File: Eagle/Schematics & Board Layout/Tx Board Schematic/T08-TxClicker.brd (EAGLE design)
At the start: 88.9 x 44.5 mm, 86 parts, among them U1 CC430F513X---RGZ48, Y1 26MHz

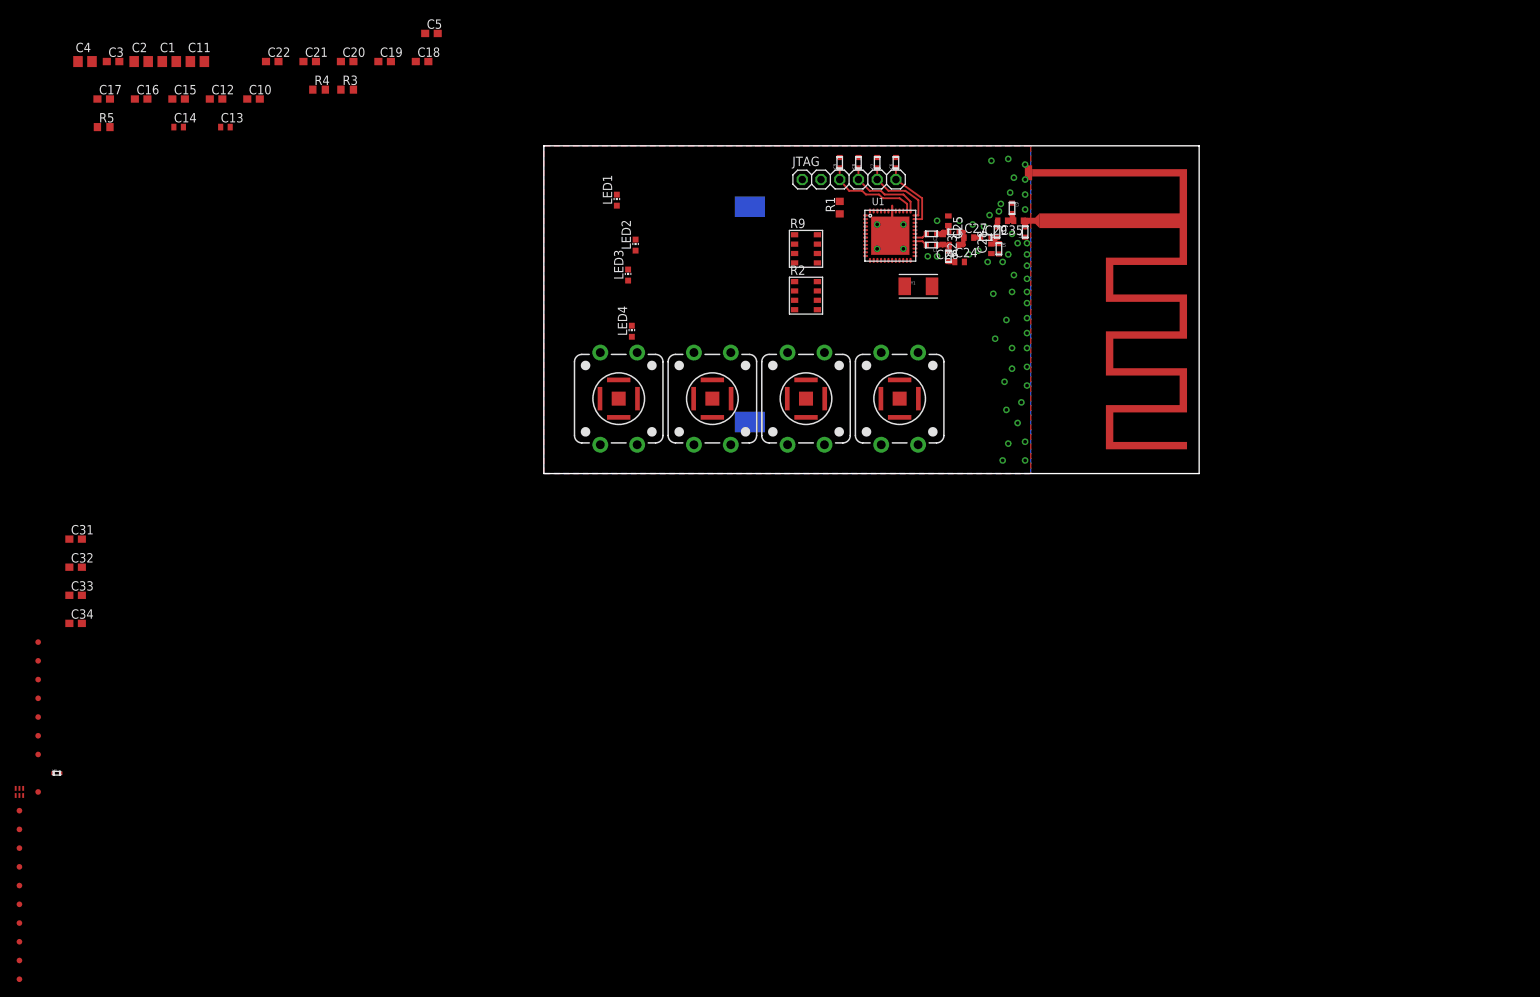
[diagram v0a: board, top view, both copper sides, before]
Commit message: Eagle BRD Layout
Incomplete, first pass layout
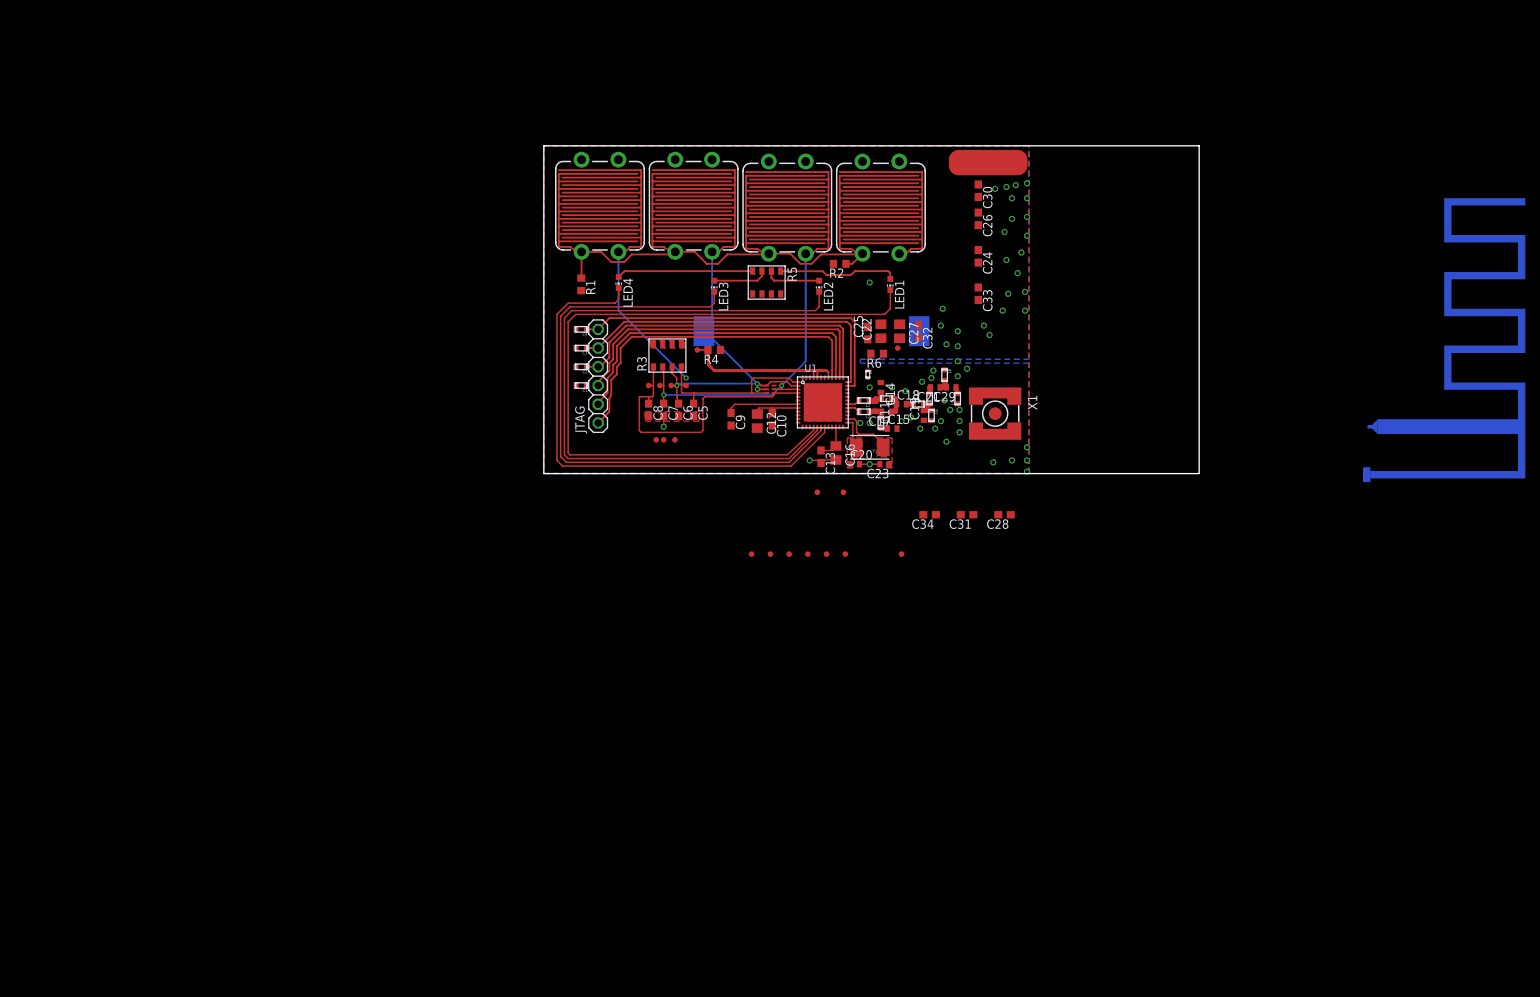
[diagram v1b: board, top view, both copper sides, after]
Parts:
- removed C35: 16pF, rcl:C0402
- removed R9: 10MEG, QuadResistor:2012(4_RES)
- removed U$1, U$3, U$4: TOUCH-PAD, TouchPad:TOUCH-PAD
- removed U$2: CR2032-SNAPDRAGONCR2032, CR2032-SnapDragon:CR2032-SNAPDRAGON
- removed U$7: PCB_ANTENNA_915MHZOSHP, PCB_Antenna_915MHz-halseth:PCB_ANTENNA_915MHZ
- added C30: 2pF, rcl:C0603
- added GND: (no value), SparkFun-Connectors:STARBOARD_GROUND_SMALL2
- added R6: 56k, rcl:R0603
- added U$6: PCB_ANTENNA_915MHZOSHP, PCB_Antenna_915MHz-halseth:PCB_ANTENNA_915MHZ
- added X1: SMA-SMD, con-coax:SMA-SMD
- C1: value 10uF -> 2nF; device rcl:C0805 -> rcl-amber:C0603
- C11: value 10uF -> 1pF; device rcl:C0805 -> rcl:C0402
- C12, C16: value 100nF -> 10uF; device rcl:C0603 -> rcl:C0805
- C13: value 18pF -> 100nF; device rcl:C0402 -> rcl:C0603
- C14: value 18pF -> 1.5pF
- C15: value 100nF -> 100pF; device rcl:C0603 -> rcl:C0402
- C17: value 2pF -> 1.5pF; device rcl:C0603 -> rcl:C0402
- C18, C21: value 100nF -> 1.5pF; device rcl:C0603 -> rcl:C0402
- C19: value 2pF -> 8.2pF; device rcl:C0603 -> rcl:C0402
- C2, C4: value 10uF -> 2pF; device rcl:C0805 -> rcl-amber:C0603
- C20: value 100nF -> 18pF; device rcl:C0603 -> rcl:C0402
- C22: value 470nF -> 10uF; device rcl:C0603 -> rcl:C0805
- C23: value 1pF -> 18pF
- C24: value 100pF -> 100nF; device rcl:C0402 -> rcl:C0603
- C25, C26: value 1.5pF -> 100nF; device rcl:C0402 -> rcl:C0603
- C27: value 1.5pF -> 10uF; device rcl:C0402 -> rcl:C0805
- C28: value 8.2pF -> 100nF; device rcl:C0402 -> rcl:C0603
- C29: value 1.5pF -> 16pF
- C3: value 100nF -> 2pF; device rcl:C0603 -> rcl-amber:C0603
- C31, C32, C33: value DNI -> 100nF
- C34: value DNI -> 2pF
- C5: value 100nF -> DNI
- C6, C7, C8: value 2pF -> DNI; device rcl-amber:C0603 -> rcl:C0603
- C9: value 2nF -> 470nF; device rcl-amber:C0603 -> rcl:C0603
- L8: value 5.6nH -> DNP
- L9: value DNP -> 5.6nH
- R1: value 47k -> 10k
- R2: value 3.3k -> DNI; device QuadResistor:2012(4_RES) -> rcl:R0603
- R3: value 56k -> 10MEG; device rcl:R0603 -> QuadResistor:2012(4_RES)
- R4: value 10k -> 47k
- R5: value DNI -> 3.3k; device rcl:R0603 -> QuadResistor:2012(4_RES)
- S1, S2, S3, S4: value SWITCH-MOMENTARY-212MM -> TOUCHPAD_SWITCH_COMBOSWITC_TOUCHPAD; device SparkFun-Electromechanical:TACTILE-PTH-12MM -> SparkFun-Electromechanical--edited:TACTILE-PTH-12MM
- U$5: value TOUCH-PAD -> CR2032-SNAPDRAGONCR2032; device TouchPad:TOUCH-PAD -> CR2032-SnapDragon:CR2032-SNAPDRAGON
- moved TP18 146.7 mm to (48.0, 17.0), turned to 90 degrees
- moved C33 129.1 mm to (58.9, 24.4), turned to 270 degrees
- moved TP9 124.6 mm to (48.5, -10.9), turned to 270 degrees
- moved L10 122.6 mm to (43.9, 13.5), turned to 270 degrees
- moved C31 120.9 mm to (57.4, -5.59), turned to 180 degrees
- moved TP10 120.8 mm to (40.6, -2.54), turned to 270 degrees
- moved TP12 119.8 mm to (40.9, -10.9), turned to 270 degrees
- moved C32 118.7 mm to (50.8, 19.3), turned to 270 degrees
- moved TP11 118.5 mm to (37.1, -2.54), turned to 270 degrees
- moved TP13 118.3 mm to (38.4, -10.9), turned to 270 degrees
- moved TP14 117.0 mm to (35.8, -10.9), turned to 270 degrees
- moved C34 116.8 mm to (52.3, -5.59), turned to 180 degrees
- moved TP15 115.8 mm to (33.3, -10.9), turned to 270 degrees
- moved D1 115.6 mm to (30.7, 11.4), turned to 270 degrees
- moved TP16 114.6 mm to (30.7, -10.9), turned to 270 degrees
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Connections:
- removed net N$10: C35.1, L8.2, U$7.ANT
- removed net N$12: TP9.P$1
- removed net N$18: LED1.A, R2.1
- removed net N$21: LED3.A, R2.7
- removed net N$23: LED4.A, R2.5
- removed net N$24: LED2.A, R2.3
- new net ANTENNA: C29.1, L9.2, U$6.ANT, X1.1
- new net N$13: LED1.A, R5.7
- new net N$14: LED2.A, R5.5
- new net N$16: LED3.A, R5.3
- new net N$17: LED4.A, R5.1
- net GND: now also C14.1, C19.1, C23.2, C25.2, C26.2, C27.2, C28.2, C30.2, R2.2, R3.2, R3.4, R3.6, R3.8, R6.1, U$5.V-, U$6.GPLANE, X1.2@1, X1.2@2, X1.2@3, X1.2@4, X1.2@5, X1.2@6; no longer C11.2, C14.2, C17.2, C18.2, C19.2, C21.2, C25.1, C28.1, R3.1, R5.2, R9.2, R9.4, R9.6, R9.8, U$2.V-, U$7.GPLANE
- net N$1: now also C11.2, C17.2, L2.1, L3.1; no longer C23.2, C26.2, L1.1, L4.1
- net N$2: now also C11.1, C14.2, L1.1, L4.2; no longer C23.1, C25.2, L2.1, L3.2
- net N$20: now also R1.1, R2.1; no longer R4.1, R5.1, U$1.P$1, U$1.P$2, U$1.P$3, U$1.P$4, U$3.P$1, U$3.P$2, U$3.P$3, U$3.P$4, U$4.P$1, U$4.P$2, U$4.P$3, U$4.P$4, U$5.P$1, U$5.P$2, U$5.P$3, U$5.P$4
- net N$3: now also C17.1, C18.1, L4.1; no longer C26.1, C27.1, L3.1
- net N$4: now also C15.1, L3.2; no longer C24.1, L4.2
- net N$5: now also C18.2; no longer C27.2
- net N$6: now also C19.2; no longer C28.2
- net N$7: now also C21.1, C29.2, L8.2; no longer C29.1, C35.2, L9.2
- net N$8: now also C21.2; no longer C29.2
- net N$9: now also C24.1, C26.1, C28.1, C30.1, C31.1, C33.1, C34.1; no longer C15.1, C16.1, C17.1, C18.1, C19.1, C20.1, C21.1
- net P1.0: no longer TP12.P$1
- net P1.1: no longer TP13.P$1
- net P1.2: no longer TP14.P$1
- net P1.3: no longer TP16.P$1
- net P1.4: no longer TP15.P$1
- net P1.5: no longer TP17.P$1
- net P1.6: no longer TP18.P$1
- net P1.7: now also C8.1, D1.4, R3.7; no longer C34.1, D1.5, R9.1, U$1.VCC
- net P2.0: now also C7.1, D1.5, R3.5; no longer C33.1, D1.4, R9.3, U$3.VCC
- net P2.1: now also C6.1, D1.1, R3.3; no longer C32.1, D1.3, R9.5, U$4.VCC
- net P2.2: now also C5.1, D1.3, R3.1; no longer C31.1, D1.1, R9.7, U$5.VCC
- net P2.6: no longer TP10.P$1
- net P2.7: no longer TP11.P$1
- net P3.2: now also LED4.C; no longer LED1.C
- net P3.3: now also LED3.C; no longer LED2.C
- net P3.4: now also LED2.C; no longer LED4.C
- net P3.5: now also LED1.C; no longer LED3.C
- net PJ.0/TDO: now also C4.1; no longer C6.1
- net PJ.1/TDI/TCLK: now also C3.1; no longer C7.1
- net PJ.2/TMS: now also C2.1; no longer C8.1
- net RF_N: now also L1.2; no longer L2.2
- net RF_P: now also L2.2; no longer L1.2
- net RF_XIN: now also C20.1; no longer C14.1
- net RF_XOUT: now also C23.1; no longer C13.1
- net RST/NMI/SBWTDIO: now also C1.1, R4.1; no longer C9.1, R1.1
- net R_BIAS: now also R6.2; no longer R3.2
- net VCC: now also C13.1, C16.1, C22.1, C25.1, C27.1, C32.1, R5.2, R5.4, R5.6, R5.8, U$5.V+; no longer C1.1, C11.1, C2.1, C3.1, C4.1, C5.1, R2.2, R2.4, R2.6, R2.8, U$2.V+
- net VCORE: now also C9.1; no longer C22.1
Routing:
- net P3.5: track 0.00 -> 99.9 mm
- net P3.4: track 0.00 -> 92.3 mm
- net P3.3: track 0.00 -> 80.0 mm
- net P3.2: track 0.00 -> 69.8 mm
- net N$20: track 0.00 -> 48.6 mm
- net P2.2: track 0.00 -> 46.4 mm, vias 0 -> 1
- net P2.0: track 0.00 -> 45.2 mm, vias 0 -> 2
- net TEST/SBWTCK: track 0.00 -> 45.1 mm
- net RST/NMI/SBWTDIO: track 1.59 -> 46.0 mm
- net P2.1: track 0.00 -> 43.6 mm, vias 0 -> 2
- net P1.7: track 0.00 -> 38.6 mm
- net PJ.0/TDO: track 9.73 -> 46.8 mm
- net VCC: track 0.00 -> 35.4 mm
- net PJ.1/TDI/TCLK: track 10.7 -> 45.7 mm
- net PJ.2/TMS: track 11.2 -> 45.2 mm
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- added copper zone on layer 1, net RF_XIN
- added copper zone on layer 1, net RF_XOUT
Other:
- board text added: "1"
- board text added: "12"
- board text added: "24"
- board text added: "36"

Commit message: Layout works
o.O
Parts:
- removed X1: SMA-SMD, con-coax:SMA-SMD
- added R7: 0-DNI, rcl-amber:R0603
- added X1-DNI: SMA-SMD, con-coax:SMA-SMD
- C11, C14, C15, C17, C18, C19, C21, C29: device rcl:C0402 -> rcl-amber:C0402
- L1, L2, L3, L4, L5, L6, L7, L8, L9: device rcl-amber:L0603 -> rcl-amber:L0402
- L10: device rcl-amber:L0402 -> rcl-amber:L0603
- moved U$6 47.5 mm to (65.6, 8.13), flipped to the top, turned to 270 degrees
- moved C30 12.9 mm to (61.0, 25.7)
- moved R1 12.8 mm to (17.8, 27.2)
- moved L8 11.2 mm to (63.5, 6.96), turned to 90 degrees
- moved C29 9.57 mm to (64.1, 8.13)
- moved L9 9.25 mm to (64.8, 6.86)
- moved C26 8.89 mm to (58.9, 25.7)
- moved C24 4.32 mm to (56.9, 25.7)
- moved C33 4.26 mm to (54.9, 25.7)
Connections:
- net N$33 renamed P5.1
- removed net N$7: C21.1, C29.2, L8.2
- new net N$10: R7.2, X1-DNI.1
- new net N$12: C21.P$1, C29.P$2, L8.P$2, R7.1
- net ANTENNA: now also C29.P$1, L9.P$2; no longer C29.1, L9.2, X1.1
- net GND: now also C14.P$1, C15.P$2, C19.P$1, L6.P$2, L8.P$1, L9.P$1, X1-DNI.2@1, X1-DNI.2@2, X1-DNI.2@3, X1-DNI.2@4, X1-DNI.2@5, X1-DNI.2@6; no longer C14.1, C15.2, C19.1, L6.2, L8.1, L9.1, X1.2@1, X1.2@2, X1.2@3, X1.2@4, X1.2@5, X1.2@6
- net N$1: now also C11.P$2, C17.P$2, L2.P$1, L3.P$1; no longer C11.2, C17.2, L2.1, L3.1
- net N$2: now also C11.P$1, C14.P$2, L1.P$1, L4.P$2; no longer C11.1, C14.2, L1.1, L4.2
- net N$3: now also C17.P$1, C18.P$1, L4.P$1; no longer C17.1, C18.1, L4.1
- net N$4: now also C15.P$1, L3.P$2; no longer C15.1, L3.2
- net N$5: now also C18.P$2, L5.P$1; no longer C18.2, L5.1
- net N$6: now also C19.P$2, L5.P$2, L6.P$1, L7.P$1; no longer C19.2, L5.2, L6.1, L7.1
- net N$8: now also C21.P$2, L7.P$2; no longer C21.2, L7.2
- net N$9: now also L10.2; no longer L10.P$2
- net RF_N: now also L1.P$2; no longer L1.2
- net RF_P: now also L2.P$2; no longer L2.2
- net VCC: now also L10.1; no longer L10.P$1
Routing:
- net P1.7: track 38.6 -> 67.3 mm, vias 0 -> 1
- net VCC: track 35.4 -> 60.0 mm, vias 0 -> 3
- net N$12: track 0.00 -> 20.0 mm
- net N$17: track 18.5 -> 25.1 mm
- net N$10: track 0.00 -> 4.15 mm
- net GND: track 9.36 -> 12.7 mm, vias 57 -> 60
- net N$20: track 48.6 -> 46.5 mm
- net N$7: track 1.89 -> 0.00 mm
- net RST/NMI/SBWTDIO: track 46.0 -> 47.8 mm
- net ANTENNA: track 0.89 -> 2.16 mm
- net N$2: track 3.06 -> 4.11 mm
- net N$11: track 0.76 -> 0.00 mm
- net N$1: track 2.70 -> 3.37 mm
- net N$6: track 3.04 -> 3.59 mm
- net N$3: track 3.08 -> 3.58 mm

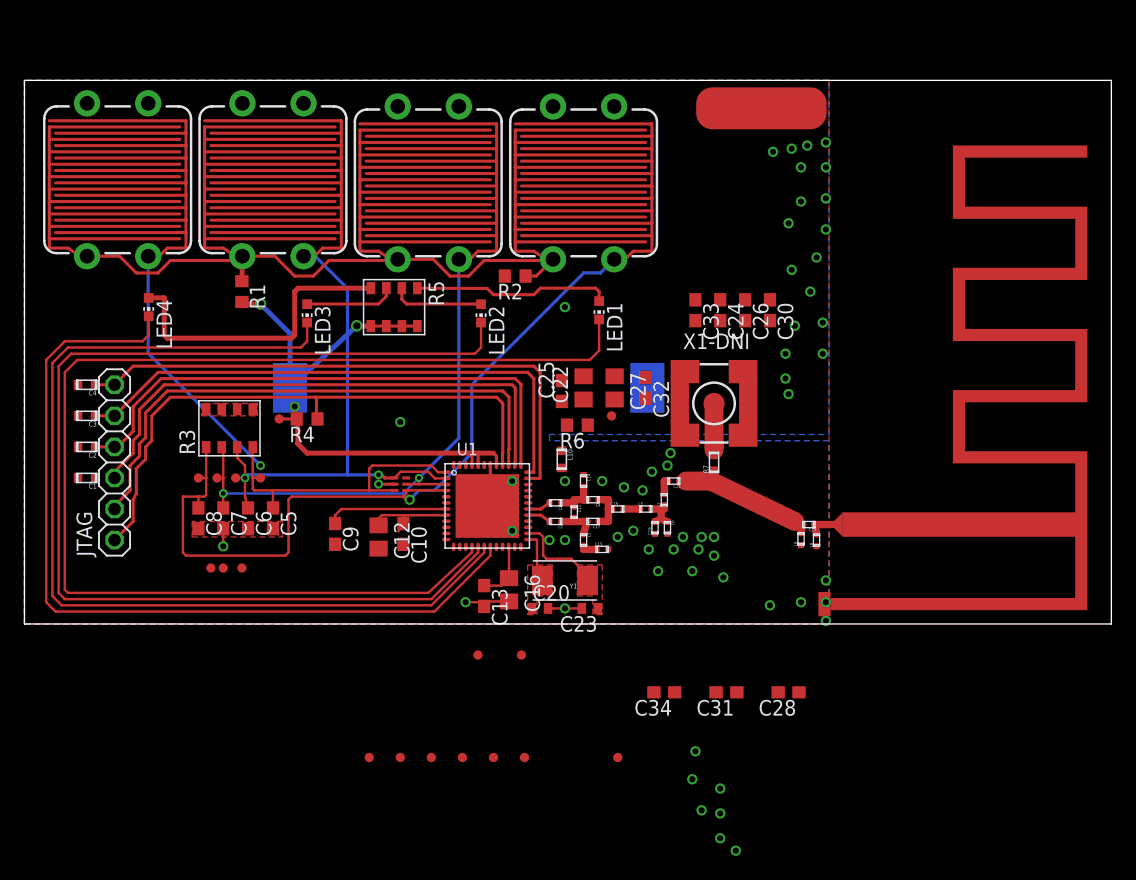
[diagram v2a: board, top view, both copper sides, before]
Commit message: Eagle BRD Layout (rough)
Squawk list:
1) Antenna Pad
2) Pushbutton pad
3) VCC
4) Capacitors not near pins
5) Must optimize routing
6) Add ground test point
7) Fix GPIO Test points in schematic
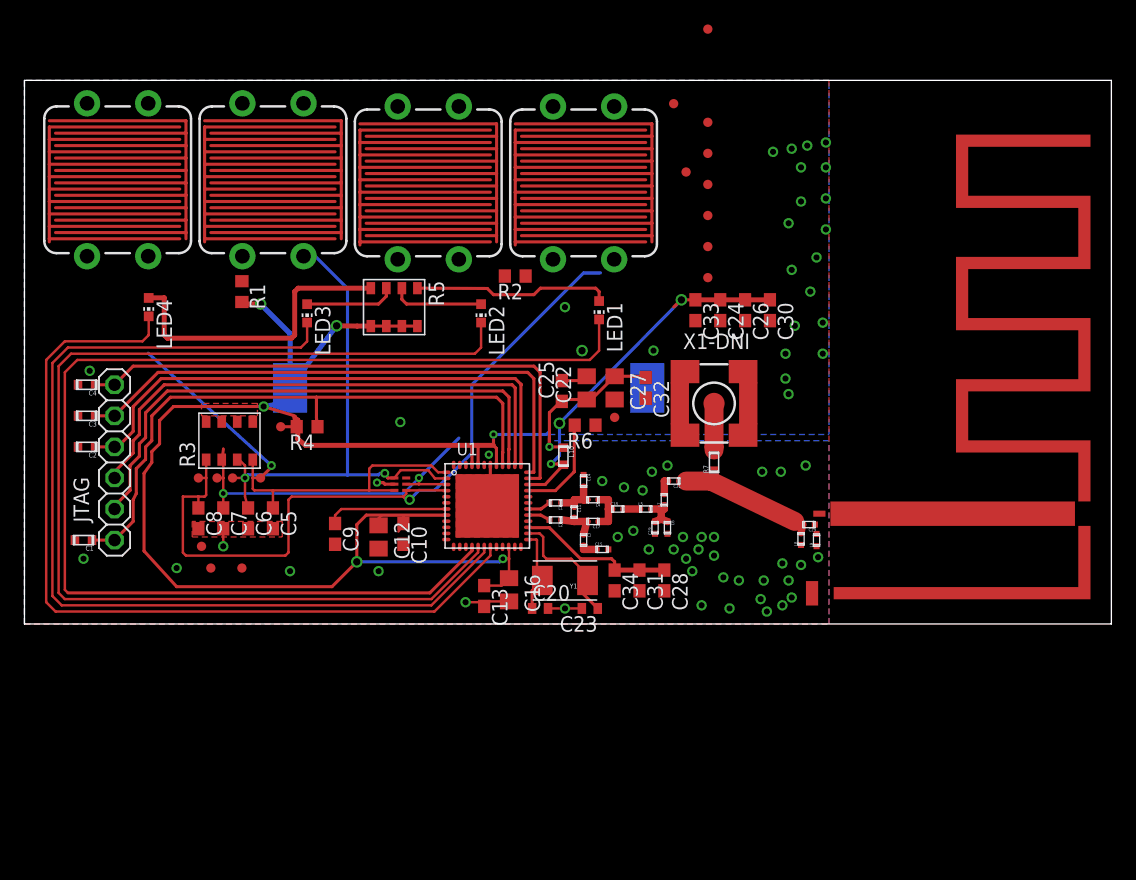
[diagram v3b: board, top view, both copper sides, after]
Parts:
- removed GND: (no value), SparkFun-Connectors:STARBOARD_GROUND_SMALL2
- S1, S2, S3, S4: value TOUCHPAD_SWITCH_COMBOSWITC_TOUCHPAD -> TOUCHPAD_SWITCH_COMBO
- moved TP9 60.0 mm to (55.9, 48.6), turned to 0 degrees
- moved TP12 54.1 mm to (55.9, 41.0), turned to 0 degrees
- moved TP13 52.4 mm to (55.9, 38.5), turned to 0 degrees
- moved TP14 51.0 mm to (55.9, 35.9), turned to 0 degrees
- moved TP15 49.8 mm to (55.9, 33.4), turned to 0 degrees
- moved TP16 48.8 mm to (55.9, 30.9), turned to 0 degrees
- moved TP17 48.0 mm to (55.9, 28.3), turned to 0 degrees
- moved TP10 46.8 mm to (53.1, 42.5), turned to 0 degrees
- moved TP11 43.0 mm to (54.1, 37.0), turned to 0 degrees
- moved C28 13.7 mm to (52.3, 3.56), turned to 270 degrees
- moved C31 11.6 mm to (50.3, 3.56), turned to 270 degrees
- moved C34 10.0 mm to (48.3, 3.56), turned to 270 degrees
- moved C1 5.09 mm to (4.83, 6.86)
- moved TP2 2.51 mm to (14.5, 6.35)
- moved R3 1.02 mm to (16.8, 15.0)
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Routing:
- net VCC: track 60.0 -> 149.8 mm, vias 3 -> 7
- net N$11: track 46.5 -> 0.00 mm
- net N$9: track 0.00 -> 43.5 mm, vias 0 -> 3
- net P2.0: track 45.2 -> 31.3 mm
- net R_BIAS: track 0.00 -> 8.21 mm
- net P2.2: track 46.4 -> 39.5 mm
- net RF_XOUT: track 6.33 -> 11.0 mm
- net RF_XIN: track 3.78 -> 6.95 mm
- net P1.7: track 67.3 -> 64.7 mm
- net RST/NMI/SBWTDIO: track 47.8 -> 50.2 mm
- net GND: track 12.7 -> 15.2 mm, vias 60 -> 63
- net ANTENNA: track 2.16 -> 0.00 mm
- net P2.1: track 43.1 -> 42.0 mm
- net P3.5: vias 0 -> 1
- removed copper zone on layer 1, net RF_XIN
- removed copper zone on layer 1, net RF_XOUT
